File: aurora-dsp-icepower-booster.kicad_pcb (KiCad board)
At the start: 2 copper layers, 200 x 200 mm, 269 parts, among them J1 XLR_IN_1, J10 XLR3_OUT, J11 XLR3_OUT, J12 XLR3_OUT, J13 24V DC, J14 REMOTE 3.5mm, J2 XLR_IN_2, J3 XLR_IN_3, J4 XLR_IN_4, J5 XLR_IN_5, J6 XLR_IN_6, J7 XLR3_OUT, J8 XLR3_OUT, J9 XLR3_OUT, Q1 BSS138, Q2 BSS138, Q3 BSS138, Q4 BSS138, Q5 BSS138, Q6 BSS138, Q7 BSS138, SW1 Gain CH1, SW2 Gain CH2, SW3 Gain CH3, SW4 Gain CH4, SW5 Gain CH5, SW6 Gain CH6, SW7 ALWAYS/REMOTE, U1 LM4562, U10 LM4562, U11 LM4562, U12 LM4562, U13 TEL5-2422, U14 ADP7118ARDZ-11, U15 ADP7182AUJZ-11, U2 LM4562, U3 LM4562, U4 LM4562, U5 LM4562, U6 LM4562, U7 LM4562, U8 LM4562, U9 LM4562

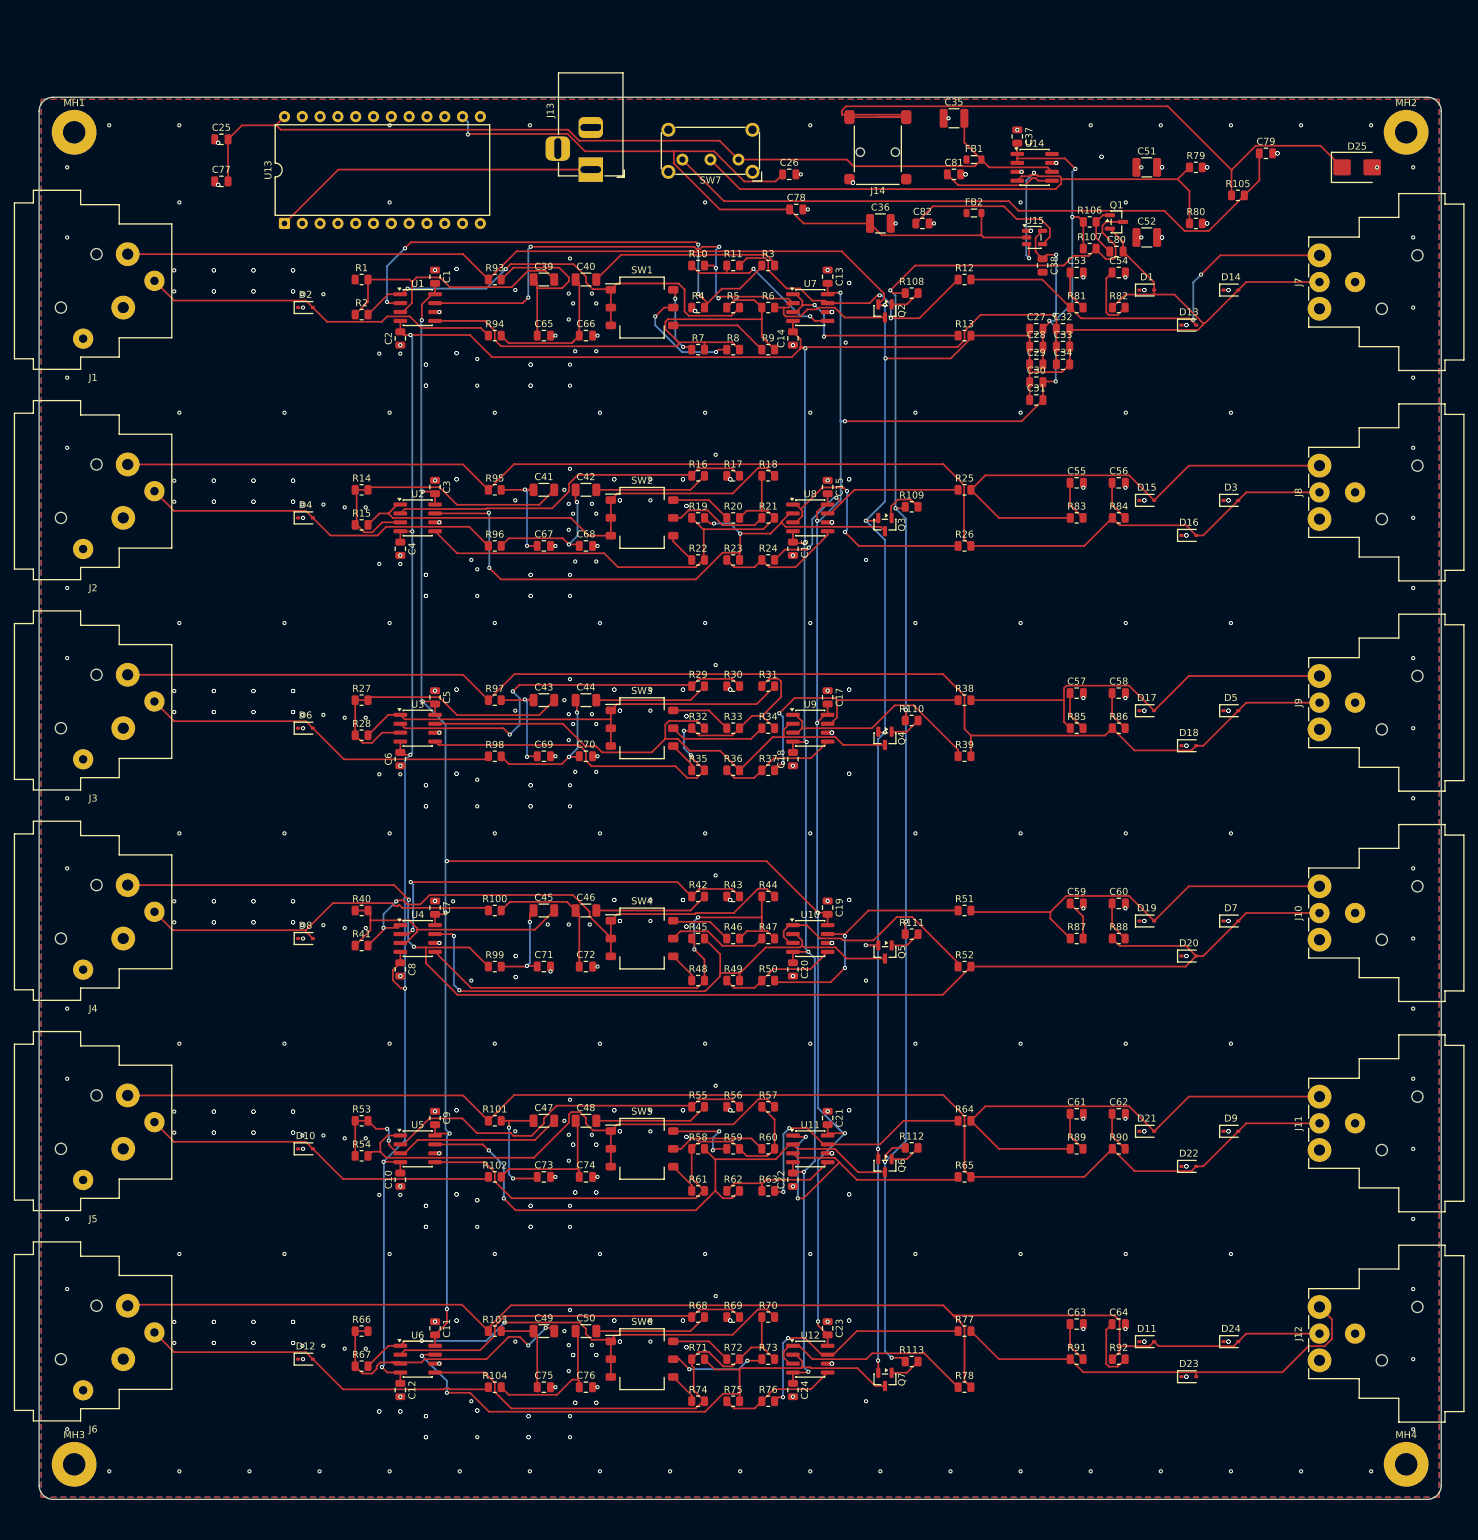
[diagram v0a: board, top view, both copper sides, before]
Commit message: PCB v3: netlist-driven placement, 0 shorts, all 239 components placed
- New build_pcb_v3.py with correct component-to-channel mapping
- J1-J6=XLR inputs, J7-J12=XLR outputs, J13=barrel, J14=remote
- U1-U6=Rx+Gain, U7-U12=Driver, U13=TEL5, U14=ADP7118, U15=ADP7182
- SW1-SW6=DIP gain switches (per channel), SW7=ALWAYS/REMOTE (PCB 'SW1')
- All fixed positions (J1-J14, SW7) preserved at user-defined locations
- 0 shorting violations, 319 unconnected (expected, no routing yet)
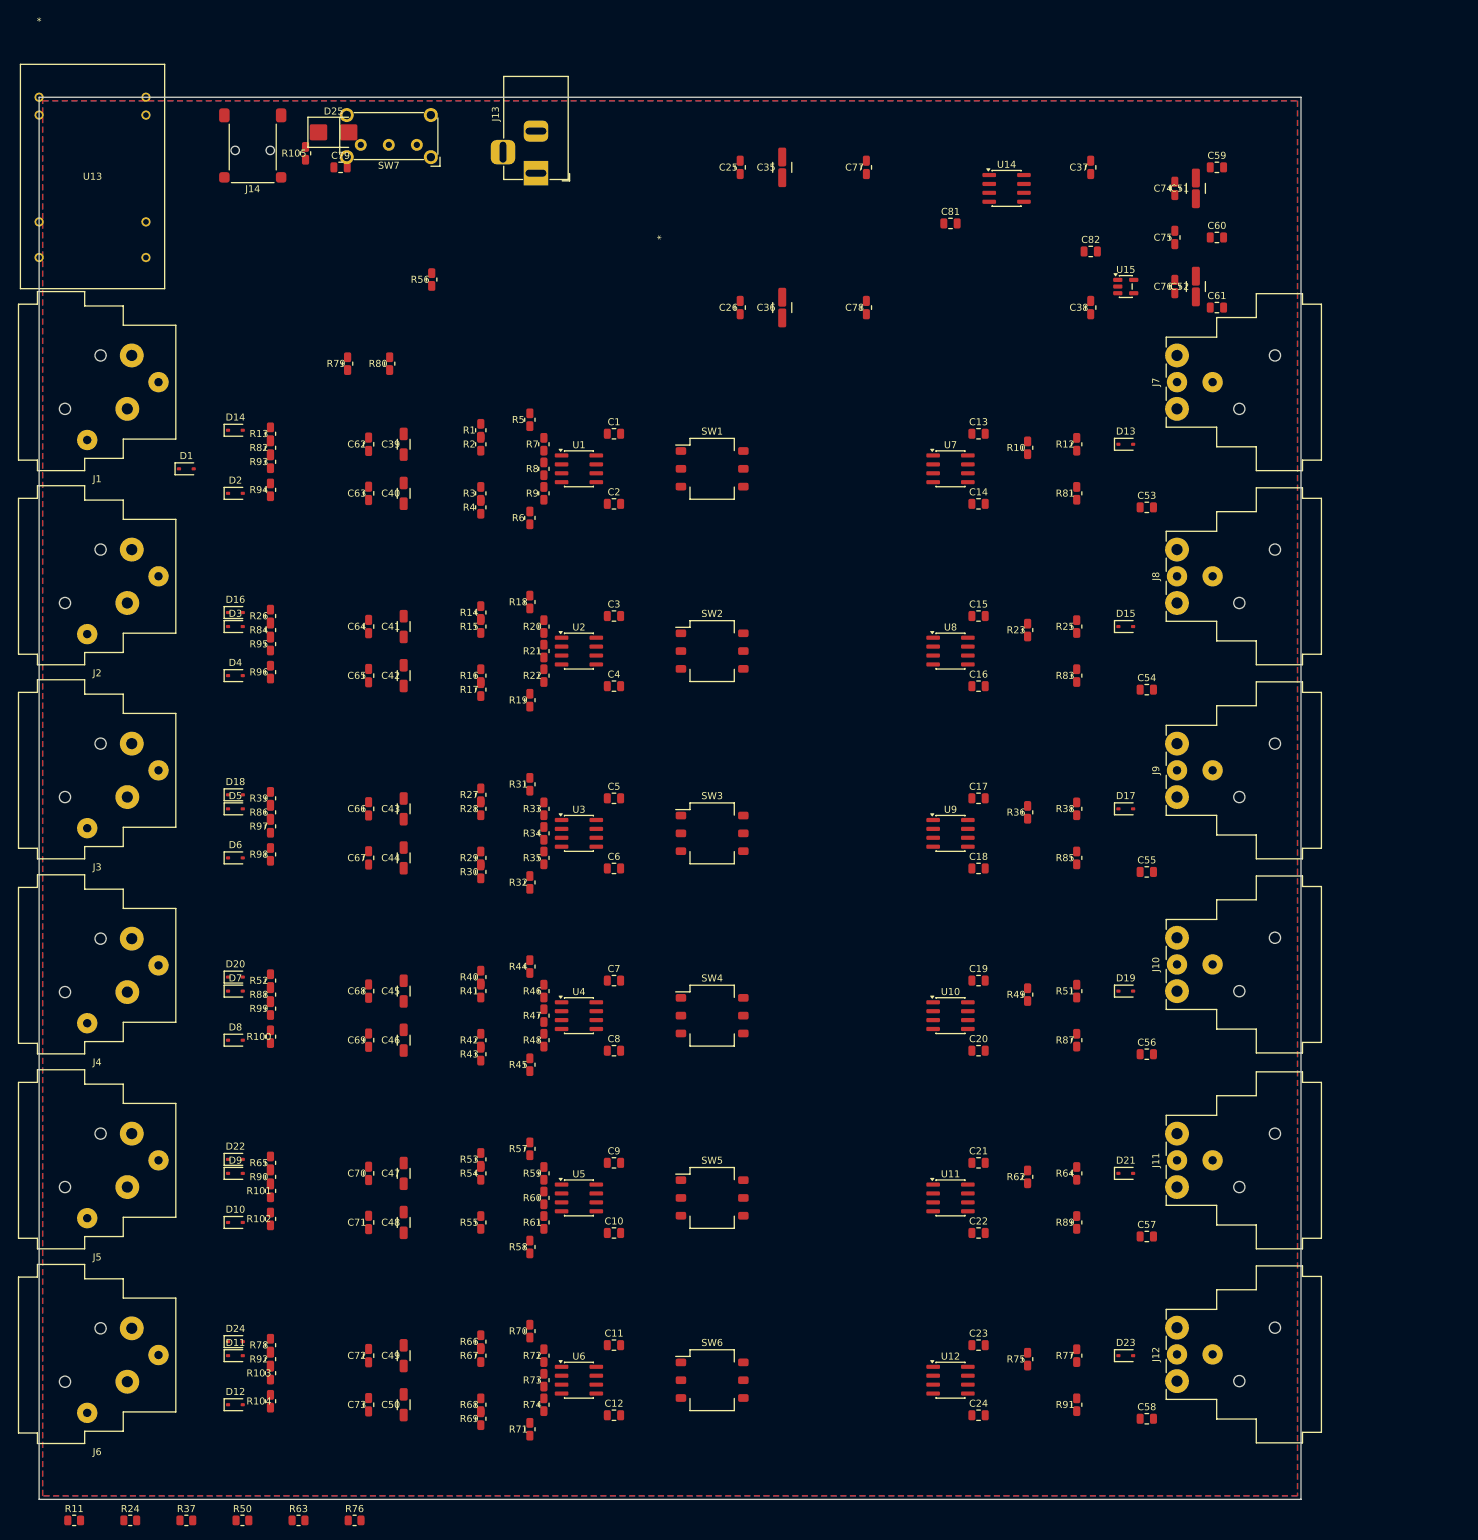
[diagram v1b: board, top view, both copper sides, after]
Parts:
- removed C27, C28, C29, C30, C31, C32, C33, C34: 100nF C0G, Capacitor_SMD:C_0805_2012Metric
- removed C80: 10u, Capacitor_SMD:C_0805_2012Metric
- removed FB1, FB2: BLM18PG221, Inductor_SMD:L_0805_2012Metric
- removed MH1, MH2, MH3, MH4: MountingHole, MountingHole:MountingHole_3.2mm_M3_Pad
- removed Q1, Q2, Q3, Q4, Q5, Q6, Q7: BSS138, Package_TO_SOT_SMD:SOT-23
- removed R106, R108, R109, R110, R111, R112, R113: 10k, Resistor_SMD:R_0805_2012Metric
- removed R107: 100k, Resistor_SMD:R_0805_2012Metric
- U13: footprint Package_DIP:DIP-24_W15.24mm -> TEL5_DUAL_TRP
- moved R11 202.2 mm to (5.00, 203.0)
- moved C75 187.1 mm to (162.0, 20.0), turned to 90 degrees
- moved C76 178.1 mm to (162.0, 27.0), turned to 90 degrees
- moved R24 164.5 mm to (13.0, 203.0)
- moved C74 164.1 mm to (162.0, 13.0), turned to 90 degrees
- moved C63 155.7 mm to (47.0, 56.5), turned to 90 degrees
- moved C64 146.1 mm to (47.0, 75.5), turned to 90 degrees
- moved D25 146.1 mm to (42.0, 5.00)
- moved C62 143.4 mm to (47.0, 49.5), turned to 90 degrees
- moved D14 143.4 mm to (28.0, 47.5)
- moved D3 143.1 mm to (28.0, 75.5)
- moved D5 142.7 mm to (28.0, 101.5)
- moved D7 142.4 mm to (28.0, 127.5)
- moved D9 142.1 mm to (28.0, 153.5)
- moved D24 142.0 mm to (28.0, 177.5)
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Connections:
- C39 pad 1: /CH1_EMI_HOT -> (no net)
- C40 pad 1: /CH1_EMI_COLD -> (no net)
- C41 pad 1: /CH2_EMI_HOT -> (no net)
- C42 pad 1: /CH2_EMI_COLD -> (no net)
- C43 pad 1: /CH3_EMI_HOT -> (no net)
- C44 pad 1: /CH3_EMI_COLD -> (no net)
- C45 pad 1: /CH4_EMI_HOT -> (no net)
- C46 pad 1: /CH4_EMI_COLD -> (no net)
- C47 pad 1: /CH5_EMI_HOT -> (no net)
- C48 pad 1: /CH5_EMI_COLD -> (no net)
- C49 pad 1: /CH6_EMI_HOT -> (no net)
- C50 pad 1: /CH6_EMI_COLD -> (no net)
- C53 pad 1: /CH1_OUT_PROT_HOT -> (no net)
- C54 pad 1: /CH1_OUT_PROT_COLD -> (no net)
- C55 pad 1: /CH2_OUT_PROT_HOT -> (no net)
- C56 pad 1: /CH2_OUT_PROT_COLD -> (no net)
- C57 pad 1: /CH3_OUT_PROT_HOT -> (no net)
- C58 pad 1: /CH3_OUT_PROT_COLD -> (no net)
- C59 pad 1: /CH4_OUT_PROT_HOT -> (no net)
- C60 pad 1: /CH4_OUT_PROT_COLD -> (no net)
- C61 pad 1: /CH5_OUT_PROT_HOT -> (no net)
- C62 pad 1: /CH5_OUT_PROT_COLD -> (no net)
- C63 pad 1: /CH6_OUT_PROT_HOT -> (no net)
- C64 pad 1: /CH6_OUT_PROT_COLD -> (no net)
- C65 pad 1: /CH1_EMI_HOT -> (no net)
- C66 pad 1: /CH1_EMI_COLD -> (no net)
- C67 pad 1: /CH2_EMI_HOT -> (no net)
- C68 pad 1: /CH2_EMI_COLD -> (no net)
- C69 pad 1: /CH3_EMI_HOT -> (no net)
- C70 pad 1: /CH3_EMI_COLD -> (no net)
- C71 pad 1: /CH4_EMI_HOT -> (no net)
- C72 pad 1: /CH4_EMI_COLD -> (no net)
- C73 pad 1: /CH5_EMI_HOT -> (no net)
- C74 pad 1: /CH5_EMI_COLD -> (no net)
- C75 pad 1: /CH6_EMI_HOT -> (no net)
- C76 pad 1: /CH6_EMI_COLD -> (no net)
- D1 pad 2: /CH1_OUT_COLD -> /CH1_HOT_RAW
- D11 pad 2: /CH6_OUT_COLD -> /CH6_HOT_RAW
- D14 pad 2: /CH1_OUT_COLD -> /CH1_HOT_RAW
- D16 pad 2: /CH2_OUT_COLD -> /CH2_HOT_RAW
- D18 pad 2: /CH3_OUT_COLD -> /CH3_HOT_RAW
- D20 pad 2: /CH4_OUT_COLD -> /CH4_HOT_RAW
- D22 pad 2: /CH5_OUT_COLD -> /CH5_HOT_RAW
- D24 pad 2: /CH6_OUT_COLD -> /CH6_HOT_RAW
- D3 pad 2: /CH2_OUT_COLD -> /CH2_HOT_RAW
- D5 pad 2: /CH3_OUT_COLD -> /CH3_HOT_RAW
- D7 pad 2: /CH4_OUT_COLD -> /CH4_HOT_RAW
- D9 pad 2: /CH5_OUT_COLD -> /CH5_HOT_RAW
- J1 pad 2: /CH1_OUT_COLD -> /CH1_HOT_RAW
- J1 pad 3: /CH1_COLD_RAW -> (no net)
- J1 pad G: /GND -> (no net)
- J10 pad 3: /CH4_OUT_COLD -> (no net)
- J11 pad 3: /CH5_OUT_COLD -> (no net)
- J12 pad 3: /CH6_OUT_COLD -> (no net)
- J2 pad 2: /CH2_OUT_COLD -> /CH2_HOT_RAW
- J2 pad 3: /CH2_COLD_RAW -> (no net)
- J2 pad G: /GND -> (no net)
- J3 pad 2: /CH3_OUT_COLD -> /CH3_HOT_RAW
- J3 pad 3: /CH3_COLD_RAW -> (no net)
- J3 pad G: /GND -> (no net)
- J4 pad 2: /CH4_OUT_COLD -> /CH4_HOT_RAW
- J4 pad 3: /CH4_COLD_RAW -> (no net)
- J4 pad G: /GND -> (no net)
- J5 pad 2: /CH5_OUT_COLD -> /CH5_HOT_RAW
- J5 pad 3: /CH5_COLD_RAW -> (no net)
- J5 pad G: /GND -> (no net)
- J6 pad 2: /CH6_OUT_COLD -> /CH6_HOT_RAW
- J6 pad 3: /CH6_COLD_RAW -> (no net)
- J6 pad G: /GND -> (no net)
- J7 pad 3: /CH1_OUT_COLD -> (no net)
- J8 pad 3: /CH2_OUT_COLD -> (no net)
- J9 pad 3: /CH3_OUT_COLD -> (no net)
- R10 pad 1: /CH1_GAIN_FB -> (no net)
- R100 pad 2: /CH4_EMI_COLD -> (no net)
- R101 pad 1: /CH5_OUT_COLD -> /CH5_HOT_RAW
- R101 pad 2: /CH5_EMI_HOT -> (no net)
- R102 pad 2: /CH5_EMI_COLD -> (no net)
- R103 pad 1: /CH6_OUT_COLD -> /CH6_HOT_RAW
- R103 pad 2: /CH6_EMI_HOT -> (no net)
- R104 pad 2: /CH6_EMI_COLD -> (no net)
- R11 pad 1: /CH1_GAIN_FB -> (no net)
- R11 pad 2: /CH1_OUT_DRIVE -> (no net)
- R12 pad 1: /CH1_OUT_DRIVE -> (no net)
- R13 pad 1: /CH1_BUF_DRIVE -> (no net)
- R13 pad 2: /CH1_OUT_COLD -> /CH1_HOT_RAW
- R15 pad 2: /CH2_RX_OUT -> (no net)
- R16 pad 1: /CH2_INV_IN -> (no net)
- R17 pad 2: /CH2_INV_IN -> (no net)
- R2 pad 2: /CH1_RX_OUT -> (no net)
- R20 pad 1: /CH2_SW_OUT_1 -> (no net)
- R21 pad 1: /CH2_SW_OUT_2 -> (no net)
- R22 pad 1: /CH2_SW_OUT_3 -> (no net)
- R23 pad 1: /CH2_GAIN_FB -> (no net)
- R24 pad 1: /CH2_GAIN_FB -> (no net)
- R24 pad 2: /CH2_OUT_DRIVE -> (no net)
- R25 pad 1: /CH2_OUT_DRIVE -> (no net)
- R26 pad 1: /CH2_BUF_DRIVE -> (no net)
- R26 pad 2: /CH2_OUT_COLD -> /CH2_HOT_RAW
- R28 pad 2: /CH3_RX_OUT -> (no net)
- R29 pad 1: /CH3_INV_IN -> (no net)
- R3 pad 1: /CH1_INV_IN -> (no net)
- R30 pad 2: /CH3_INV_IN -> (no net)
- R33 pad 1: /CH3_SW_OUT_1 -> (no net)
- R34 pad 1: /CH3_SW_OUT_2 -> (no net)
- R35 pad 1: /CH3_SW_OUT_3 -> (no net)
- R36 pad 1: /CH3_GAIN_FB -> (no net)
- R37 pad 1: /CH3_GAIN_FB -> (no net)
- R37 pad 2: /CH3_OUT_DRIVE -> (no net)
- R38 pad 1: /CH3_OUT_DRIVE -> (no net)
- R39 pad 1: /CH3_BUF_DRIVE -> (no net)
- R39 pad 2: /CH3_OUT_COLD -> /CH3_HOT_RAW
- R4 pad 2: /CH1_INV_IN -> (no net)
- R41 pad 2: /CH4_RX_OUT -> (no net)
- R42 pad 1: /CH4_INV_IN -> (no net)
- R43 pad 2: /CH4_INV_IN -> (no net)
- R46 pad 1: /CH4_SW_OUT_1 -> (no net)
- R47 pad 1: /CH4_SW_OUT_2 -> (no net)
- R48 pad 1: /CH4_SW_OUT_3 -> (no net)
- R49 pad 1: /CH4_GAIN_FB -> (no net)
- R50 pad 1: /CH4_GAIN_FB -> (no net)
- R50 pad 2: /CH4_OUT_DRIVE -> (no net)
- R51 pad 1: /CH4_OUT_DRIVE -> (no net)
- R52 pad 1: /CH4_BUF_DRIVE -> (no net)
- R52 pad 2: /CH4_OUT_COLD -> /CH4_HOT_RAW
- R54 pad 2: /CH5_RX_OUT -> (no net)
- R55 pad 1: /CH5_INV_IN -> (no net)
- R56 pad 2: /CH5_INV_IN -> (no net)
- R59 pad 1: /CH5_SW_OUT_1 -> (no net)
- R60 pad 1: /CH5_SW_OUT_2 -> (no net)
- R61 pad 1: /CH5_SW_OUT_3 -> (no net)
- R62 pad 1: /CH5_GAIN_FB -> (no net)
- R63 pad 1: /CH5_GAIN_FB -> (no net)
- R63 pad 2: /CH5_OUT_DRIVE -> (no net)
- R64 pad 1: /CH5_OUT_DRIVE -> (no net)
- R65 pad 1: /CH5_BUF_DRIVE -> (no net)
- R65 pad 2: /CH5_OUT_COLD -> /CH5_HOT_RAW
- R67 pad 2: /CH6_RX_OUT -> (no net)
- R68 pad 1: /CH6_INV_IN -> (no net)
- R69 pad 2: /CH6_INV_IN -> (no net)
- R7 pad 1: /CH1_SW_OUT_1 -> (no net)
- R72 pad 1: /CH6_SW_OUT_1 -> (no net)
- R73 pad 1: /CH6_SW_OUT_2 -> (no net)
- R74 pad 1: /CH6_SW_OUT_3 -> (no net)
- R75 pad 1: /CH6_GAIN_FB -> (no net)
- R76 pad 1: /CH6_GAIN_FB -> (no net)
- R76 pad 2: /CH6_OUT_DRIVE -> (no net)
- R77 pad 1: /CH6_OUT_DRIVE -> (no net)
- R78 pad 1: /CH6_BUF_DRIVE -> (no net)
- R78 pad 2: /CH6_OUT_COLD -> /CH6_HOT_RAW
- R8 pad 1: /CH1_SW_OUT_2 -> (no net)
- R81 pad 2: /CH1_OUT_PROT_HOT -> (no net)
- R82 pad 1: /CH1_OUT_COLD -> /CH1_HOT_RAW
- R82 pad 2: /CH1_OUT_PROT_COLD -> (no net)
- R83 pad 2: /CH2_OUT_PROT_HOT -> (no net)
- R84 pad 1: /CH2_OUT_COLD -> /CH2_HOT_RAW
- R84 pad 2: /CH2_OUT_PROT_COLD -> (no net)
- R85 pad 2: /CH3_OUT_PROT_HOT -> (no net)
- R86 pad 1: /CH3_OUT_COLD -> /CH3_HOT_RAW
- R86 pad 2: /CH3_OUT_PROT_COLD -> (no net)
- R87 pad 2: /CH4_OUT_PROT_HOT -> (no net)
- R88 pad 1: /CH4_OUT_COLD -> /CH4_HOT_RAW
- R88 pad 2: /CH4_OUT_PROT_COLD -> (no net)
- R89 pad 2: /CH5_OUT_PROT_HOT -> (no net)
- R9 pad 1: /CH1_SW_OUT_3 -> (no net)
- R90 pad 1: /CH5_OUT_COLD -> /CH5_HOT_RAW
- R90 pad 2: /CH5_OUT_PROT_COLD -> (no net)
- R91 pad 2: /CH6_OUT_PROT_HOT -> (no net)
- R92 pad 1: /CH6_OUT_COLD -> /CH6_HOT_RAW
- R92 pad 2: /CH6_OUT_PROT_COLD -> (no net)
- R93 pad 1: /CH1_OUT_COLD -> /CH1_HOT_RAW
- R93 pad 2: /CH1_EMI_HOT -> (no net)
- R94 pad 2: /CH1_EMI_COLD -> (no net)
- R95 pad 1: /CH2_OUT_COLD -> /CH2_HOT_RAW
- R95 pad 2: /CH2_EMI_HOT -> (no net)
- R96 pad 2: /CH2_EMI_COLD -> (no net)
- R97 pad 1: /CH3_OUT_COLD -> /CH3_HOT_RAW
- R97 pad 2: /CH3_EMI_HOT -> (no net)
- R98 pad 2: /CH3_EMI_COLD -> (no net)
- R99 pad 1: /CH4_OUT_COLD -> /CH4_HOT_RAW
- R99 pad 2: /CH4_EMI_HOT -> (no net)
- SW1 pad 4: /CH1_SW_OUT_3 -> (no net)
- SW1 pad 5: /CH1_SW_OUT_2 -> (no net)
- SW1 pad 6: /CH1_SW_OUT_1 -> (no net)
- SW2 pad 4: /CH2_SW_OUT_3 -> (no net)
- SW2 pad 5: /CH2_SW_OUT_2 -> (no net)
- SW2 pad 6: /CH2_SW_OUT_1 -> (no net)
- SW3 pad 4: /CH3_SW_OUT_3 -> (no net)
- SW3 pad 5: /CH3_SW_OUT_2 -> (no net)
- SW3 pad 6: /CH3_SW_OUT_1 -> (no net)
- SW4 pad 4: /CH4_SW_OUT_3 -> (no net)
- SW4 pad 5: /CH4_SW_OUT_2 -> (no net)
- SW4 pad 6: /CH4_SW_OUT_1 -> (no net)
- SW5 pad 4: /CH5_SW_OUT_3 -> (no net)
- SW5 pad 5: /CH5_SW_OUT_2 -> (no net)
- SW5 pad 6: /CH5_SW_OUT_1 -> (no net)
- SW6 pad 4: /CH6_SW_OUT_3 -> (no net)
- SW6 pad 5: /CH6_SW_OUT_2 -> (no net)
- SW6 pad 6: /CH6_SW_OUT_1 -> (no net)
- U1 pad 1: /CH1_RX_OUT -> (no net)
- U1 pad 2: /CH1_INV_IN -> (no net)
- U1 pad 4: /V- -> (no net)
- U1 pad 8: /V+ -> (no net)
- U10 pad 1: /CH4_BUF_DRIVE -> (no net)
- U10 pad 3: /CH4_BUF_DRIVE -> (no net)
- U10 pad 4: /V- -> (no net)
- U10 pad 5: /CH4_GAIN_FB -> (no net)
- U10 pad 7: /CH4_OUT_DRIVE -> (no net)
- U10 pad 8: /V+ -> (no net)
- U11 pad 1: /CH5_BUF_DRIVE -> (no net)
- U11 pad 3: /CH5_BUF_DRIVE -> (no net)
- U11 pad 4: /V- -> (no net)
- U11 pad 5: /CH5_GAIN_FB -> (no net)
- U11 pad 7: /CH5_OUT_DRIVE -> (no net)
- U11 pad 8: /V+ -> (no net)
- U12 pad 1: /CH6_BUF_DRIVE -> (no net)
- U12 pad 3: /CH6_BUF_DRIVE -> (no net)
- U12 pad 4: /V- -> (no net)
- U12 pad 5: /CH6_GAIN_FB -> (no net)
- U12 pad 7: /CH6_OUT_DRIVE -> (no net)
- U12 pad 8: /V+ -> (no net)
- U2 pad 1: /CH2_RX_OUT -> (no net)
- U2 pad 2: /CH2_INV_IN -> (no net)
- U2 pad 4: /V- -> (no net)
- U2 pad 8: /V+ -> (no net)
- U3 pad 1: /CH3_RX_OUT -> (no net)
- U3 pad 2: /CH3_INV_IN -> (no net)
- U3 pad 4: /V- -> (no net)
- U3 pad 8: /V+ -> (no net)
- U4 pad 1: /CH4_RX_OUT -> (no net)
- U4 pad 2: /CH4_INV_IN -> (no net)
- U4 pad 4: /V- -> (no net)
- U4 pad 8: /V+ -> (no net)
- U5 pad 1: /CH5_RX_OUT -> (no net)
- U5 pad 2: /CH5_INV_IN -> (no net)
- U5 pad 4: /V- -> (no net)
- U5 pad 8: /V+ -> (no net)
- U6 pad 1: /CH6_RX_OUT -> (no net)
- U6 pad 2: /CH6_INV_IN -> (no net)
- U6 pad 4: /V- -> (no net)
- U6 pad 8: /V+ -> (no net)
- U7 pad 1: /CH1_BUF_DRIVE -> (no net)
- U7 pad 3: /CH1_BUF_DRIVE -> (no net)
- U7 pad 4: /V- -> (no net)
- U7 pad 5: /CH1_GAIN_FB -> (no net)
- U7 pad 7: /CH1_OUT_DRIVE -> (no net)
- U7 pad 8: /V+ -> (no net)
- U8 pad 1: /CH2_BUF_DRIVE -> (no net)
- U8 pad 3: /CH2_BUF_DRIVE -> (no net)
- U8 pad 4: /V- -> (no net)
- U8 pad 5: /CH2_GAIN_FB -> (no net)
- U8 pad 7: /CH2_OUT_DRIVE -> (no net)
- U8 pad 8: /V+ -> (no net)
- U9 pad 1: /CH3_BUF_DRIVE -> (no net)
- U9 pad 3: /CH3_BUF_DRIVE -> (no net)
- U9 pad 4: /V- -> (no net)
- U9 pad 5: /CH3_GAIN_FB -> (no net)
- U9 pad 7: /CH3_OUT_DRIVE -> (no net)
- U9 pad 8: /V+ -> (no net)
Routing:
- net /V+: track 491.1 -> 0.00 mm, vias 18 -> 0
- net /V-: track 463.4 -> 0.00 mm, vias 14 -> 0
- net /CH1_OUT_COLD: track 389.2 -> 0.00 mm, vias 7 -> 0
- net /MUTE: track 212.2 -> 0.00 mm, vias 6 -> 0
- net /CH4_OUT_COLD: track 209.3 -> 0.00 mm, vias 2 -> 0
- net /CH6_OUT_COLD: track 192.7 -> 0.00 mm
- net /CH5_OUT_COLD: track 188.2 -> 0.00 mm
- net /CH2_OUT_COLD: track 187.6 -> 0.00 mm
- net /CH3_OUT_COLD: track 187.0 -> 0.00 mm
- net /+12V: track 136.5 -> 0.00 mm
- net /-12V: track 110.6 -> 0.00 mm, vias 1 -> 0
- net /REMOTE_IN: track 103.8 -> 0.00 mm
- net /EN_CTRL: track 101.0 -> 0.00 mm, vias 2 -> 0
- net /REMOTE_FILT: track 93.4 -> 0.00 mm
- net /CH1_GAIN_OUT: track 88.3 -> 0.00 mm, vias 5 -> 0
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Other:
- board size 200 x 200 mm -> 180 x 200 mm
